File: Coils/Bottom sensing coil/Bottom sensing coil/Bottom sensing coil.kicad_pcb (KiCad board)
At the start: 2 copper layers, 74.8 x 56.5 mm, 6 parts, among them J1 Conn_01x04

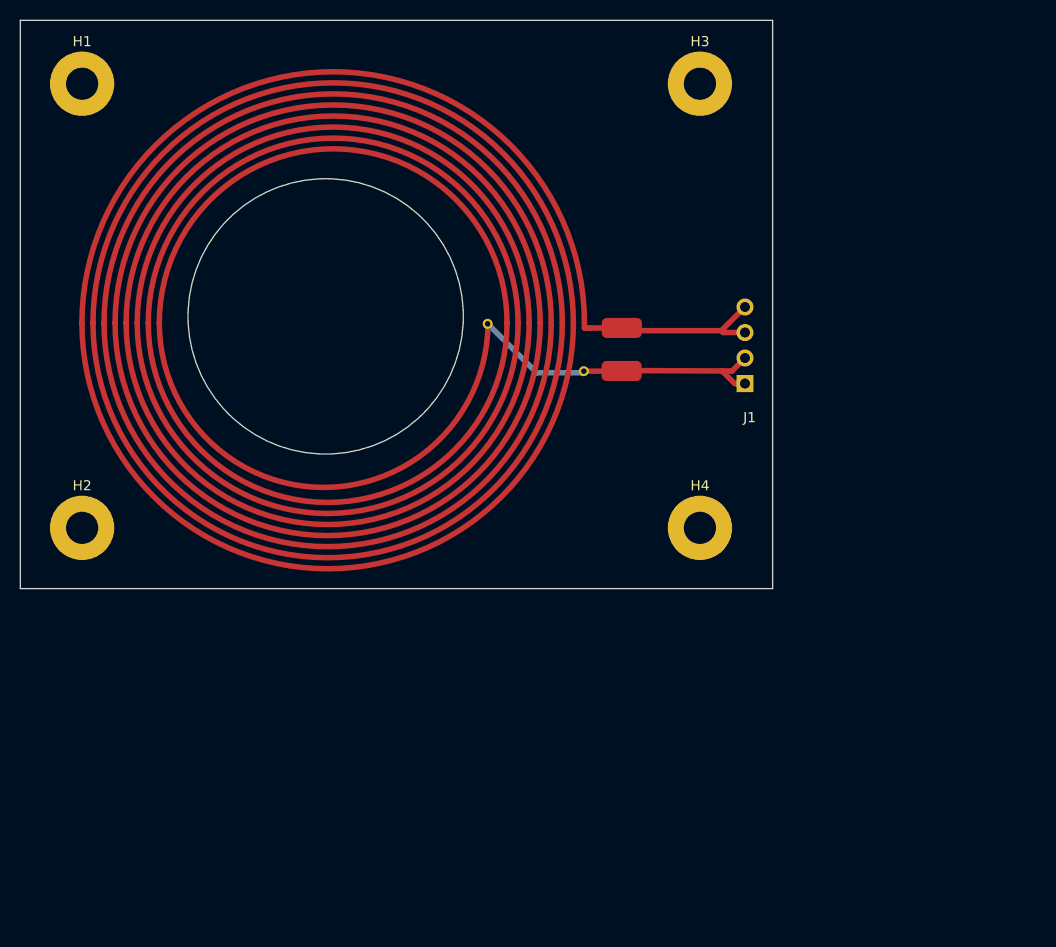
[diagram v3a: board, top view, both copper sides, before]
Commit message: Drew a footprint for a BNC edge connector 112640, made sure coils are centered and as symmetrical as possible:wq
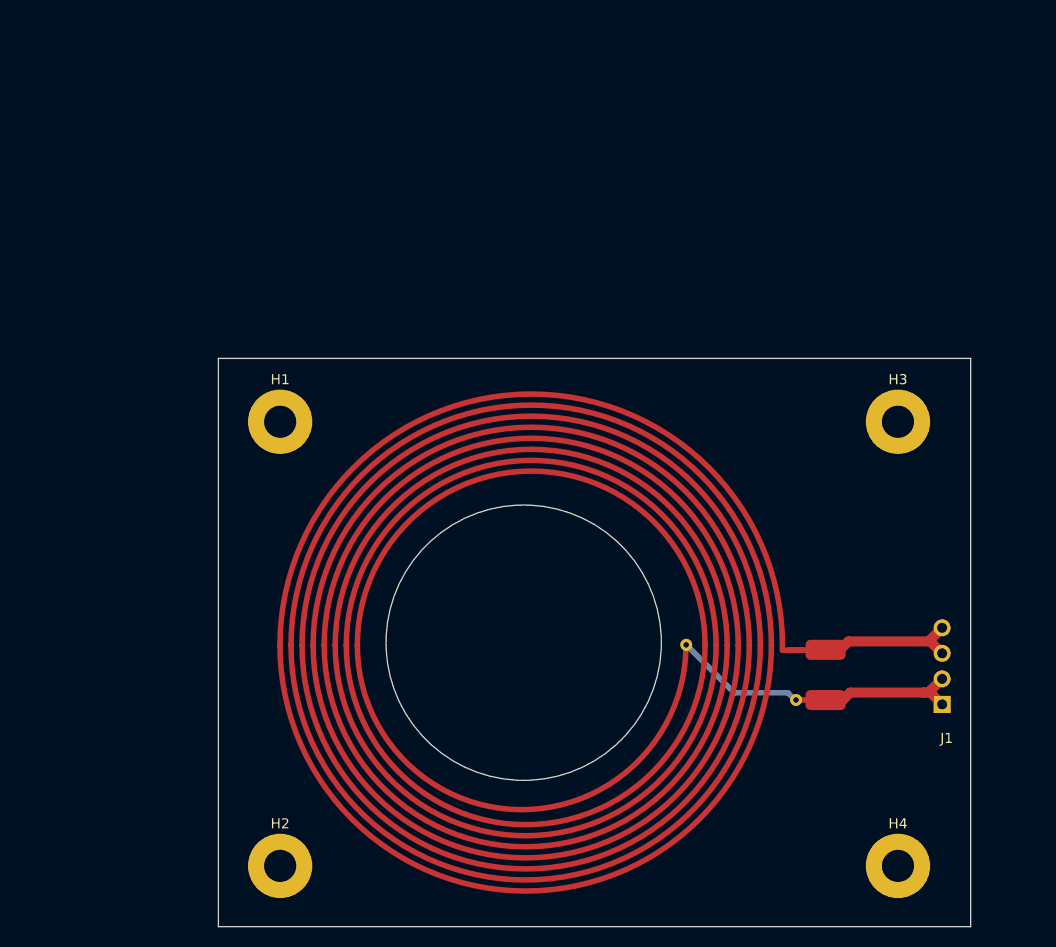
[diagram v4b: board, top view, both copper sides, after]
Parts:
- moved H3 39.0 mm to (205.0, 105.0)
- moved H4 39.0 mm to (205.0, 149.2)
- moved H1 39.0 mm to (143.5, 105.0)
- moved H2 39.0 mm to (143.5, 149.2)
- moved REF** 37.6 mm to (167.9, 127.2)
- moved J1 37.5 mm to (209.4, 133.1)
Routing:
- net /coil end: track 15.7 -> 14.3 mm
- net /coil start: track 15.4 -> 14.3 mm
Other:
- board size 74.8 x 56.5 mm -> 74.9 x 56.5 mm
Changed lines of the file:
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@@
 	(footprint "MountingHole:MountingHole_3.2mm_M3_Pad"
 		(layer "F.Cu")
-		(at 123.7968 71.3648)
+		(at 143.5 105)
 		(descr "Mounting Hole 3.2mm, M3")
 		(tags "mounting hole 3.2mm m3")
@@
 	(footprint "MountingHole:MountingHole_3.2mm_M3_Pad"
 		(layer "F.Cu")
-		(at 123.7968 115.5548)
+		(at 143.5 149.19)
 		(descr "Mounting Hole 3.2mm, M3")
 		(tags "mounting hole 3.2mm m3")
@@
 	(footprint "Top sensing coik"
 		(layer "F.Cu")
-		(at 148.225 95.175)
+		(at 167.9282 127.24)
 		(property "Reference" "REF**"
 			(at 0 0 0)
@@
 		(net_tie_pad_groups "1,2,3")
 		(fp_line
-			(start 25.51 4.79)
-			(end 27.7 4.79)
-			(stroke
-				(width 0.55)
-				(type default)
-			)
-			(layer "F.Cu")
-		)
-		(fp_line
 			(start 25.55 0)
 			(end 25.55 0.5)
@@
 				(width 0.55)
 				(type solid)
+			)
+			(layer "F.Cu")
+		)
+		(fp_line
+			(start 26.29 0.48)
+			(end 29.11 0.48)
+			(stroke
+				(width 0.55)
+				(type default)
+			)
+			(layer "F.Cu")
+		)
+		(fp_line
+			(start 26.9 5.44)
+			(end 29.1 5.44)
+			(stroke
+				(width 0.55)
+				(type default)
 			)
 			(layer "F.Cu")
@@
 		)
 		(fp_line
-			(start 15.92 0.08)
-			(end 20.79 4.95)
+			(start 20.745971 4.725971)
+			(end 16.04 0.02)
 			(stroke
 				(width 0.55)
@@
 		)
 		(fp_line
-			(start 20.79 4.95)
-			(end 25.53 4.95)
+			(start 26.11 4.74)
+			(end 20.79 4.74)
 			(stroke
 				(width 0.55)
@@
 			(layer "B.Cu")
 		)
+		(fp_line
+			(start 26.11 4.74)
+			(end 26.9 5.53)
+			(stroke
+				(width 0.55)
+				(type default)
+			)
+			(layer "B.Cu")
+		)
 		(pad "1" smd roundrect
-			(at 29.27 0.49)
+			(at 29.84 0.45)
 			(size 4 2)
 			(layers "F.Cu")
@@
 		)
 		(pad "2" smd roundrect
-			(at 29.25 4.77)
+			(at 29.84 5.45)
 			(size 4 2)
 			(layers "F.Cu")
@@
 		)
 		(pad "3" thru_hole circle
-			(at 15.92 0.08 270)
-			(size 1 1)
+			(at 15.97 -0.05 90)
+			(size 1.2 1.2)
 			(drill 0.55)
 			(layers "*.Cu" "*.Mask")
@@
 		)
 		(pad "3" thru_hole circle
-			(at 25.49 4.79 270)
-			(size 1 1)
+			(at 26.9 5.44 90)
+			(size 1.2 1.2)
 			(drill 0.55)
 			(layers "*.Cu" "*.Mask")
@@
 	(footprint "MountingHole:MountingHole_3.2mm_M3_Pad"
 		(layer "F.Cu")
-		(at 185.2668 71.3648)
+		(at 204.97 105)
 		(descr "Mounting Hole 3.2mm, M3")
 		(tags "mounting hole 3.2mm m3")
@@
 	(footprint "MountingHole:MountingHole_3.2mm_M3_Pad"
 		(layer "F.Cu")
-		(at 185.2668 115.5548)
+		(at 204.97 149.19)
 		(descr "Mounting Hole 3.2mm, M3")
 		(tags "mounting hole 3.2mm m3")
@@
 	(footprint "Connector_PinHeader_2.54mm:PinHeader_1x04_P2.54mm_Horizontal"
 		(layer "B.Cu")
-		(at 189.75 101.2)
+		(at 209.365 133.12)
 		(descr "Through hole angled pin header, 1x04, 2.54mm pitch, 6mm pin length, single row")
 		(tags "Through hole angled pin header THT 1x04 2.54mm single row")
@@
 	)
 	(gr_rect
-		(start 117.65 65.0596)
-		(end 192.5 121.6)
+		(start 137.3532 98.6948)
+		(end 212.2032 155.2352)
 		(stroke
 			(width 0.05)
@@
 	)
 	(gr_circle
-		(center 148.0284 94.513808)
-		(end 160.2668 88.3648)
+		(center 167.7316 126.98)
+		(end 179.97 120.830992)
 		(stroke
 			(width 0.05)
@@
 		(layer "Edge.Cuts")
 	)
+	(dimension
+		(type aligned)
+		(layer "User.1")
+		(pts
+			(xy 212.2032 98.6948) (xy 137.3532 98.6948)
+		)
+		(height 34.8348)
+		(gr_text "74.8500 mm"
+			(at 174.7782 62.71 0)
+			(layer "User.1")
+			(effects
+				(font
+					(size 1 1)
+					(thickness 0.15)
+				)
+			)
+		)
+		(format
+			(prefix "")
+			(suffix "")
+			(units 3)
+			(units_format 1)
+			(precision 4)
+		)
+		(style
+			(thickness 0.1)
+			(arrow_length 1.27)
+			(text_position_mode 0)
+			(extension_height 0.58642)
+			(extension_offset 0.5) keep_text_aligned)
+	)
+	(dimension
+		(type aligned)
+		(layer "User.1")
+		(pts
+			(xy 137.3532 98.6948) (xy 137.3532 155.2352)
+		)
+		(height 39.6832)
+		(gr_text "56.5404 mm"
+			(at 96.52 126.965 90)
+			(layer "User.1")
+			(effects
+				(font
+					(size 1 1)
+					(thickness 0.15)
+				)
+			)
+		)
+		(format
+			(prefix "")
+			(suffix "")
+			(units 3)
+			(units_format 1)
+			(precision 4)
+		)
+		(style
+			(thickness 0.1)
+			(arrow_length 1.27)
+			(text_position_mode 0)
+			(extension_height 0.58642)
+			(extension_offset 0.5) keep_text_aligned)
+	)
 	(segment
-		(start 187.43 99.945)
-		(end 187.45 99.925)
-		(width 0.55)
+		(start 208.115 131.87)
+		(end 208.115 131.83)
+		(width 1)
 		(layer "F.Cu")
 		(net 1)
 	)
 	(segment
-		(start 188.465 99.945)
-		(end 189.75 98.66)
-		(width 0.55)
+		(start 197.7682 132.69)
+		(end 199.475 132.69)
+		(width 1)
 		(layer "F.Cu")
 		(net 1)
 	)
 	(segment
-		(start 187.45 99.925)
-		(end 188.725 101.2)
-		(width 0.55)
+		(start 209.365 133.12)
+		(end 208.115 131.87)
+		(width 1)
 		(layer "F.Cu")
 		(net 1)
 	)
 	(segment
-		(start 188.725 101.2)
-		(end 189.75 101.2)
-		(width 0.55)
+		(start 208.115 131.83)
+		(end 208.07 131.875)
+		(width 1)
 		(layer "F.Cu")
 		(net 1)
 	)
 	(segment
-		(start 177.475 99.9)
-		(end 187.43 99.945)
-		(width 0.55)
+		(start 207.51 131.945)
+		(end 208.07 131.945)
+		(width 1)
 		(layer "F.Cu")
 		(net 1)
 	)
 	(segment
-		(start 187.43 99.945)
-		(end 188.465 99.945)
-		(width 0.55)
+		(start 208.07 131.875)
+		(end 208.07 131.945)
+		(width 1)
 		(layer "F.Cu")
 		(net 1)
 	)
 	(segment
-		(start 187.395 95.935)
-		(end 189.75 93.58)
-		(width 0.55)
+		(start 199.475 132.69)
+		(end 200.22 131.945)
+		(width 1)
+		(layer "F.Cu")
+		(net 1)
+	)
+	(segment
+		(start 209.365 130.58)
+		(end 208.115 131.83)
+		(width 1)
+		(layer "F.Cu")
+		(net 1)
+	)
+	(segment
+		(start 200.22 131.945)
+		(end 207.51 131.945)
+		(width 1)
+		(layer "F.Cu")
+		(net 1)
+	)
+	(segment
+		(start 207.51 131.945)
+		(end 207.52 131.955)
+		(width 1)
+		(layer "F.Cu")
+		(net 1)
+	)
+	(segment
+		(start 197.7682 127.69)
+		(end 199.2091 127.69)
+		(width 1)
 		(layer "F.Cu")
 		(net 2)
 	)
 	(segment
-		(start 187.58 96.12)
-		(end 189.75 96.12)
-		(width 0.55)
+		(start 199.2091 127.69)
+		(end 200.0441 126.855)
+		(width 1)
 		(layer "F.Cu")
 		(net 2)
 	)
 	(segment
-		(start 187.395 95.935)
-		(end 187.58 96.12)
-		(width 0.55)
+		(start 208.01 126.855)
+		(end 209.365 125.5)
+		(width 1)
 		(layer "F.Cu")
 		(net 2)
 	)
 	(segment
-		(start 177.765 95.935)
-		(end 187.395 95.935)
-		(width 0.55)
+		(start 200.0441 126.855)
+		(end 208.18 126.855)
+		(width 1)
 		(layer "F.Cu")
 		(net 2)
+	)
+	(segment
+		(start 208.18 126.855)
+		(end 209.365 128.04)
+		(width 1)
+		(layer "F.Cu")
+		(net 2)

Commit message: Final version before review 3
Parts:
- moved H1 8.20 mm to (150.0, 100.0)
- moved H2 8.20 mm to (150.0, 144.2)
- moved H3 8.20 mm to (211.5, 100.0)
- moved H4 8.20 mm to (211.5, 144.2)
- moved J1 8.20 mm to (215.9, 128.1)
- moved REF** 8.20 mm to (174.4, 122.2)
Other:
- board size 74.9 x 56.5 mm -> 74.8 x 56.5 mm
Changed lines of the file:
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@@
 	(footprint "MountingHole:MountingHole_3.2mm_M3_Pad"
 		(layer "F.Cu")
-		(at 143.5 105)
+		(at 150 100)
 		(descr "Mounting Hole 3.2mm, M3")
 		(tags "mounting hole 3.2mm m3")
@@
 	(footprint "MountingHole:MountingHole_3.2mm_M3_Pad"
 		(layer "F.Cu")
-		(at 143.5 149.19)
+		(at 150 144.19)
 		(descr "Mounting Hole 3.2mm, M3")
 		(tags "mounting hole 3.2mm m3")
@@
 	(footprint "Top sensing coik"
 		(layer "F.Cu")
-		(at 167.9282 127.24)
+		(at 174.4282 122.24)
 		(property "Reference" "REF**"
 			(at 0 0 0)
@@
 	(footprint "MountingHole:MountingHole_3.2mm_M3_Pad"
 		(layer "F.Cu")
-		(at 204.97 105)
+		(at 211.47 100)
 		(descr "Mounting Hole 3.2mm, M3")
 		(tags "mounting hole 3.2mm m3")
@@
 	(footprint "MountingHole:MountingHole_3.2mm_M3_Pad"
 		(layer "F.Cu")
-		(at 204.97 149.19)
+		(at 211.47 144.19)
 		(descr "Mounting Hole 3.2mm, M3")
 		(tags "mounting hole 3.2mm m3")
@@
 	(footprint "Connector_PinHeader_2.54mm:PinHeader_1x04_P2.54mm_Horizontal"
 		(layer "B.Cu")
-		(at 209.365 133.12)
+		(at 215.865 128.12)
 		(descr "Through hole angled pin header, 1x04, 2.54mm pitch, 6mm pin length, single row")
 		(tags "Through hole angled pin header THT 1x04 2.54mm single row")
@@
 		)
 	)
-	(gr_rect
-		(start 137.3532 98.6948)
-		(end 212.2032 155.2352)
+	(gr_arc
+		(start 212.50385 93.689473)
+		(mid 216.86 95.49385)
+		(end 218.664377 99.85)
 		(stroke
 			(width 0.05)
 			(type default)
 		)
-		(fill none)
 		(layer "Edge.Cuts")
 	)
-	(gr_circle
-		(center 167.7316 126.98)
-		(end 179.97 120.830992)
+	(gr_line
+		(start 150 93.689473)
+		(end 212.50385 93.689473)
 		(stroke
 			(width 0.05)
 			(type default)
 		)
+		(layer "Edge.Cuts")
+	)
+	(gr_arc
+		(start 143.839473 99.85)
+		(mid 145.64385 95.49385)
+		(end 150 93.689473)
+		(stroke
+			(width 0.05)
+			(type default)
+		)
+		(layer "Edge.Cuts")
+	)
+	(gr_circle
+		(center 174.2316 121.98)
+		(end 186.47 115.830992)
+		(stroke
+			(width 0.05)
+			(type default)
+		)
 		(fill none)
+		(layer "Edge.Cuts")
+	)
+	(gr_line
+		(start 143.839473 144.03)
+		(end 143.839473 99.85)
+		(stroke
+			(width 0.05)
+			(type default)
+		)
+		(layer "Edge.Cuts")
+	)
+	(gr_arc
+		(start 150 150.190527)
+		(mid 145.643849 148.38615)
+		(end 143.839473 144.03)
+		(stroke
+			(width 0.05)
+			(type default)
+		)
+		(layer "Edge.Cuts")
+	)
+	(gr_line
+		(start 218.664377 99.85)
+		(end 218.664377 144.03)
+		(stroke
+			(width 0.05)
+			(type default)
+		)
+		(layer "Edge.Cuts")
+	)
+	(gr_arc
+		(start 218.664377 144.03)
+		(mid 216.86 148.38615)
+		(end 212.50385 150.190527)
+		(stroke
+			(width 0.05)
+			(type default)
+		)
+		(layer "Edge.Cuts")
+	)
+	(gr_line
+		(start 150 150.190527)
+		(end 212.50385 150.190527)
+		(stroke
+			(width 0.05)
+			(type default)
+		)
 		(layer "Edge.Cuts")
 	)
@@
 	)
 	(segment
-		(start 208.115 131.87)
-		(end 208.115 131.83)
+		(start 214.615 126.87)
+		(end 214.615 126.83)
 		(width 1)
 		(layer "F.Cu")
@@
 	)
 	(segment
-		(start 197.7682 132.69)
-		(end 199.475 132.69)
+		(start 204.2682 127.69)
+		(end 205.975 127.69)
 		(width 1)
 		(layer "F.Cu")
@@
 	)
 	(segment
-		(start 209.365 133.12)
-		(end 208.115 131.87)
+		(start 215.865 128.12)
+		(end 214.615 126.87)
 		(width 1)
 		(layer "F.Cu")
@@
 	)
 	(segment
-		(start 208.115 131.83)
-		(end 208.07 131.875)
+		(start 214.615 126.83)
+		(end 214.57 126.875)
 		(width 1)
 		(layer "F.Cu")
@@
 	)
 	(segment
-		(start 207.51 131.945)
-		(end 208.07 131.945)
+		(start 214.01 126.945)
+		(end 214.57 126.945)
 		(width 1)
 		(layer "F.Cu")
@@
 	)
 	(segment
-		(start 208.07 131.875)
-		(end 208.07 131.945)
+		(start 214.57 126.875)
+		(end 214.57 126.945)
 		(width 1)
 		(layer "F.Cu")
@@
 	)
 	(segment
-		(start 199.475 132.69)
-		(end 200.22 131.945)
+		(start 205.975 127.69)
+		(end 206.72 126.945)
 		(width 1)
 		(layer "F.Cu")
@@
 	)
 	(segment
-		(start 209.365 130.58)
-		(end 208.115 131.83)
+		(start 215.865 125.58)
+		(end 214.615 126.83)
 		(width 1)
 		(layer "F.Cu")
@@
 	)
 	(segment
-		(start 200.22 131.945)
-		(end 207.51 131.945)
+		(start 206.72 126.945)
+		(end 214.01 126.945)
 		(width 1)
 		(layer "F.Cu")
@@
 	)
 	(segment
-		(start 207.51 131.945)
-		(end 207.52 131.955)
+		(start 214.01 126.945)
+		(end 214.02 126.955)
 		(width 1)
 		(layer "F.Cu")
@@
 	)
 	(segment
-		(start 197.7682 127.69)
-		(end 199.2091 127.69)
+		(start 204.2682 122.69)
+		(end 205.7091 122.69)
 		(width 1)
 		(layer "F.Cu")
@@
 	)
 	(segment
-		(start 199.2091 127.69)
-		(end 200.0441 126.855)
+		(start 205.7091 122.69)
+		(end 206.5441 121.855)
 		(width 1)
 		(layer "F.Cu")
@@
 	)
 	(segment
-		(start 208.01 126.855)
-		(end 209.365 125.5)
+		(start 214.51 121.855)
+		(end 215.865 120.5)
 		(width 1)
 		(layer "F.Cu")
@@
 	)
 	(segment
-		(start 200.0441 126.855)
-		(end 208.18 126.855)
+		(start 206.5441 121.855)
+		(end 214.68 121.855)
 		(width 1)
 		(layer "F.Cu")
@@
 	)
 	(segment
-		(start 208.18 126.855)
-		(end 209.365 128.04)
+		(start 214.68 121.855)
+		(end 215.865 123.04)
 		(width 1)
 		(layer "F.Cu")
 		(net 2)
 	)
+	(group ""
+		(members "2312ce2a-6d41-444f-a2f8-a5b571b082cf" "4618dd87-75d7-4880-a4fb-6504777968ae"
+			"748682be-81bc-4c4a-ba6f-5856fdc0633f" "86412682-aa86-47b8-b1b3-435ace1c97cf"
+			"c07d41e5-0ed7-4730-9a6e-ce113b651b02" "c1d59315-d3ae-439a-b8e6-71e72aae6f10"
+			"c7d868d3-3d95-4f19-b574-a68ebfdfd5f0" "f918484e-1661-4c98-a174-c9333d791303"
+		)
+	)
 )
